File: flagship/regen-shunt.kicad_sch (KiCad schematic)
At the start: 18 parts, among them J3 EXT_SHUNT, Q501 PSMN3R7-100BSE, U3 TLV1805, U4 TLV431

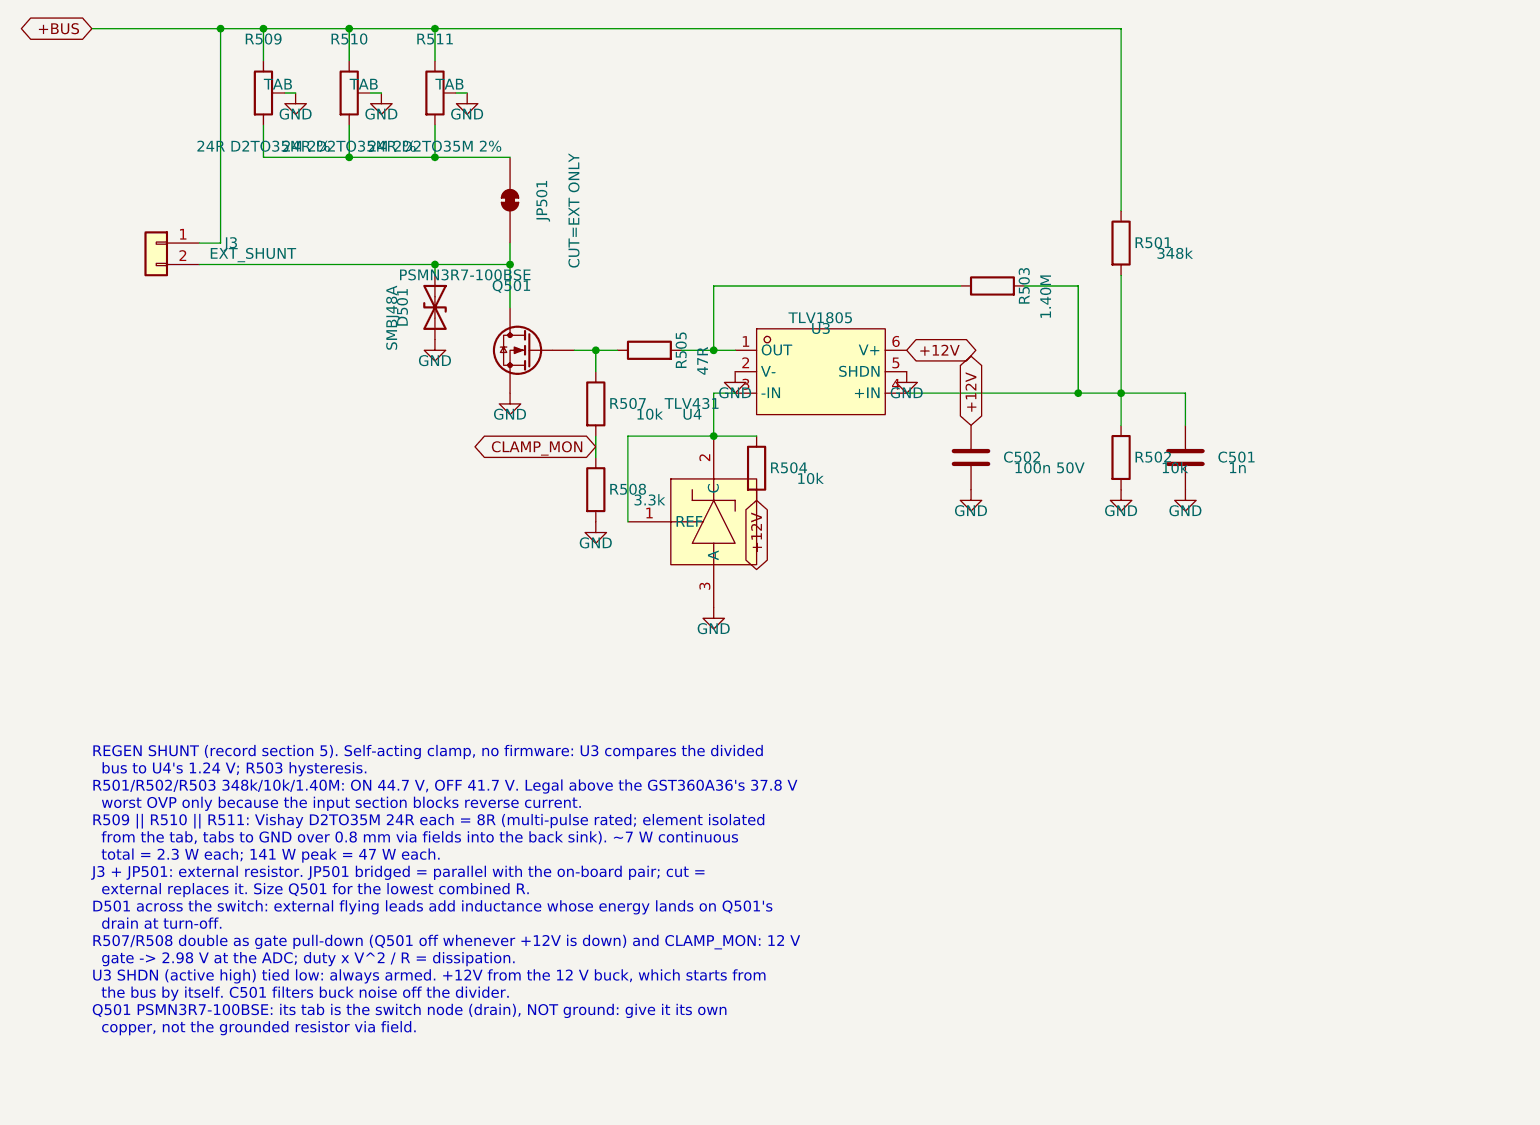
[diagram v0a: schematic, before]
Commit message: flagship: regen clamp revised -- UCC27517 driver, 1.4 V hysteresis, SS310 freewheel, clamp LED, CLAMP_MON counting, shunt NTC
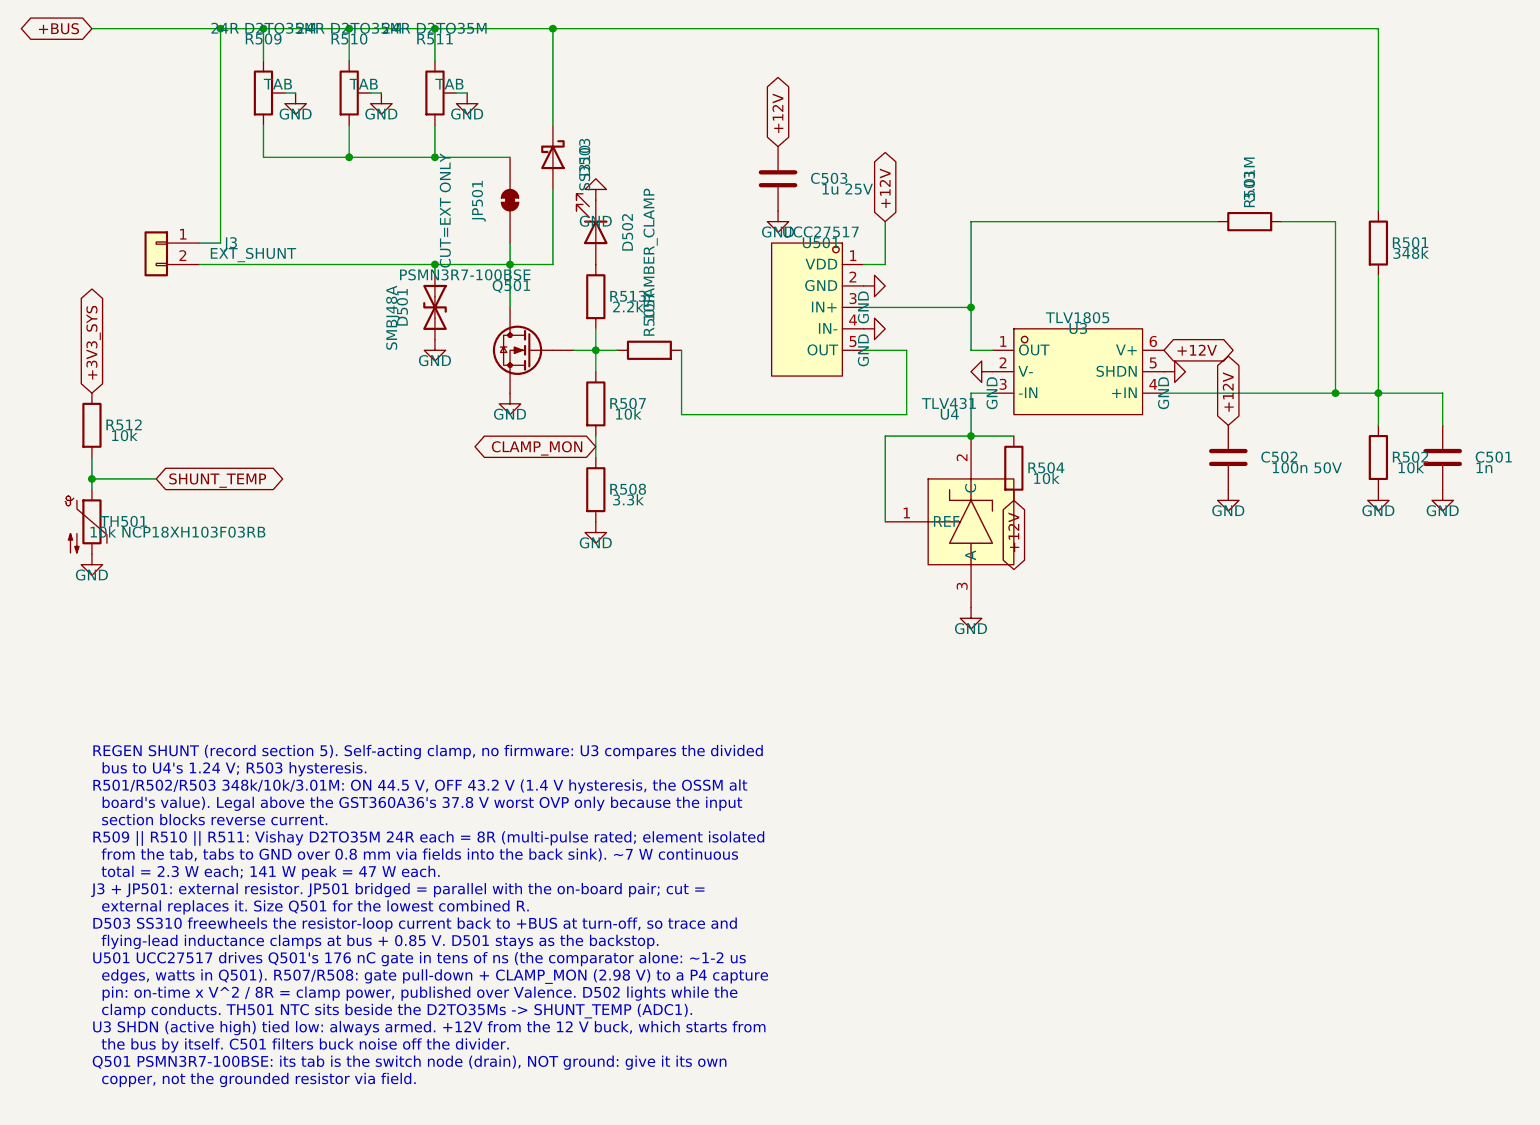
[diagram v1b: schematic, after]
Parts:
- added C503: 1u 25V, Capacitor_SMD:C_0805_2012Metric, symbol Device:C
- added D502: AMBER_CLAMP, LED_SMD:LED_0805_2012Metric, symbol Device:LED
- added D503: SS310, Diode_SMD:D_SMA, symbol Device:D_Schottky
- added R512: 10k, Resistor_SMD:R_0805_2012Metric, symbol Device:R
- added R513: 2.2k, Resistor_SMD:R_0805_2012Metric, symbol Device:R
- added TH501: 10k NCP18XH103F03RB, Resistor_SMD:R_0603_1608Metric, symbol Device:Thermistor_NTC
- added U501: UCC27517, flagship:SOT-23-5_L3.0-W1.7-P0.95-LS2.8-BR, symbol flagship:UCC27517DBVR
- R503: value 1.40M -> 3.01M
- R505: value 47R -> 10R
- R509, R510, R511: value 24R D2TO35M 2% -> 24R D2TO35M
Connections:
- net +12V: now also C503.1, U501.1 (VDD)
- net +BUS: now also D503.1 (K)
- net GND: now also C503.2, D502.1 (K), TH501.2, U501.2 (GND), U501.4 (IN-)
- net at Q501.1 (G), R505.1, R507.1: now also R513.2
- net at R503.1, U3.1 (OUT): now also U501.3 (IN+); no longer R505.2
- net at D501.1 (A1), J3.2 (Pin_2), JP501.1 (A)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: now also D503.2 (A)
- new net: R505.2, U501.5 (OUT)
- new net: D502.2 (A), R513.1
- new net +3V3_SYS: R512.1
- new net SHUNT_TEMP: R512.2, TH501.1
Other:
- note added: "REGEN SHUNT (record section 5). Self-acting clamp, no firmware: U3 compares the divided bus to U4's 1.24 V; R503 hysteresis. R501/R502/R503 348k/10k/3.01M: ON 44.5 V, OFF 43.2 V (1.4 V hysteresis, the OSSM alt board's value). Legal above the GST360A36's 37.8 V worst OVP only because the input section blocks reverse current. R509 || R510 || R511: Vishay D2TO35M 24R each = 8R (multi-pulse rated; el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"
- note removed: "REGEN SHUNT (record section 5). Self-acting clamp, no firmware: U3 compares the divided bus to U4's 1.24 V; R503 hysteresis. R501/R502/R503 348k/10k/1.40M: ON 44.7 V, OFF 41.7 V. Legal above the GST360A36's 37.8 V worst OVP only because the input section blocks reverse current. R509 || R510 || R511: Vishay D2TO35M 24R each = 8R (multi-pulse rated; element isolated from the tab, tabs to GND over 0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"

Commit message: flagship: drop the regen gate driver -- TLV1805 drives Q501 directly; switching loss ~0.16 W, not watts
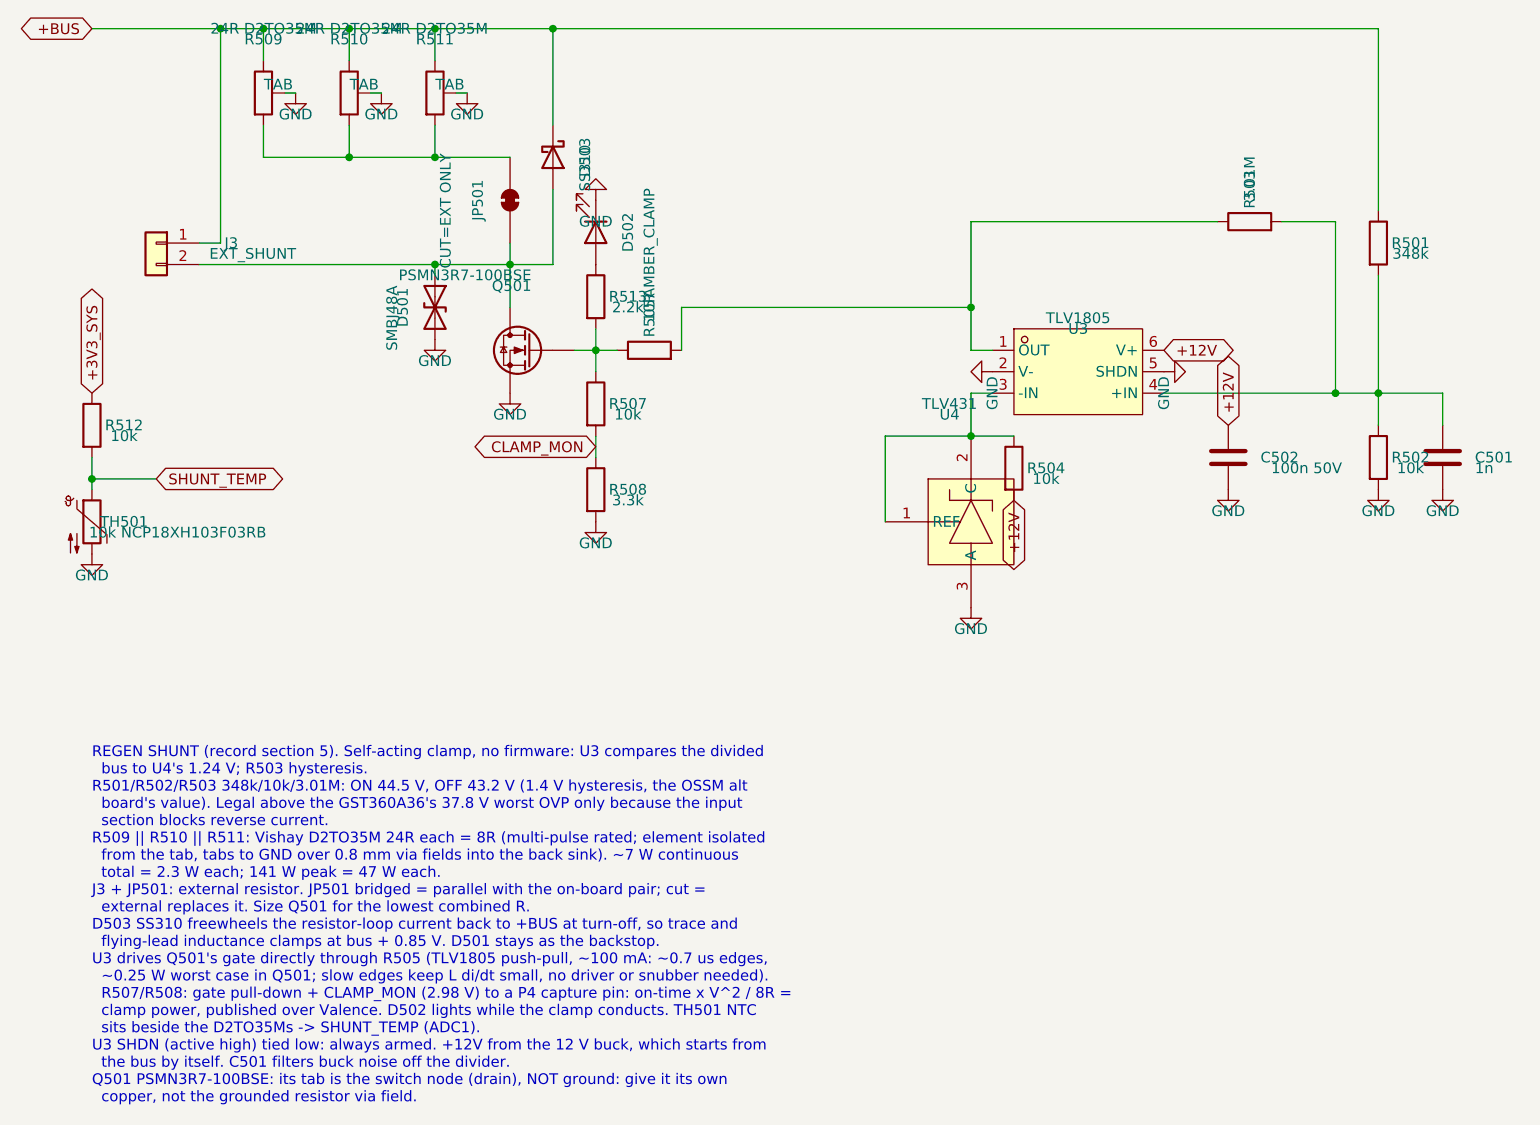
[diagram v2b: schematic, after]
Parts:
- removed C503: 1u 25V, Capacitor_SMD:C_0805_2012Metric, symbol Device:C
- removed U501: UCC27517, flagship:SOT-23-5_L3.0-W1.7-P0.95-LS2.8-BR, symbol flagship:UCC27517DBVR
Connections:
- net at R503.1, U3.1 (OUT): now also R505.2
